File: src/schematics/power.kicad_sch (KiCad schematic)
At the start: 43 parts, among them U1 L6981NDR, U2 L6981NDR, U3 ST1S41PHR, U4 L6981NDR, U5 LM3880

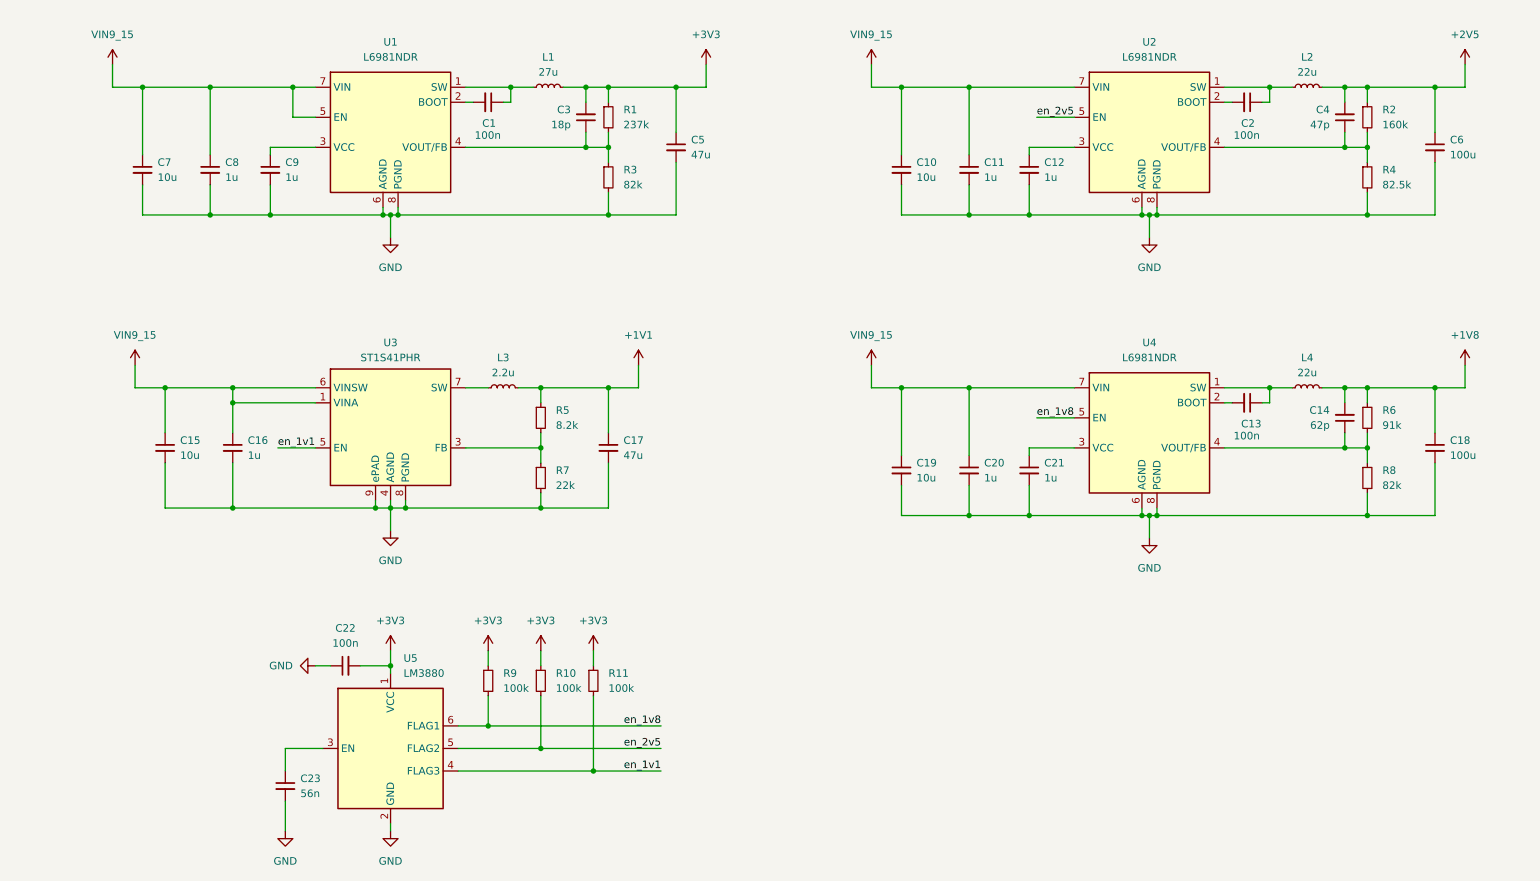
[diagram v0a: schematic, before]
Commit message: Fix some ERC issues
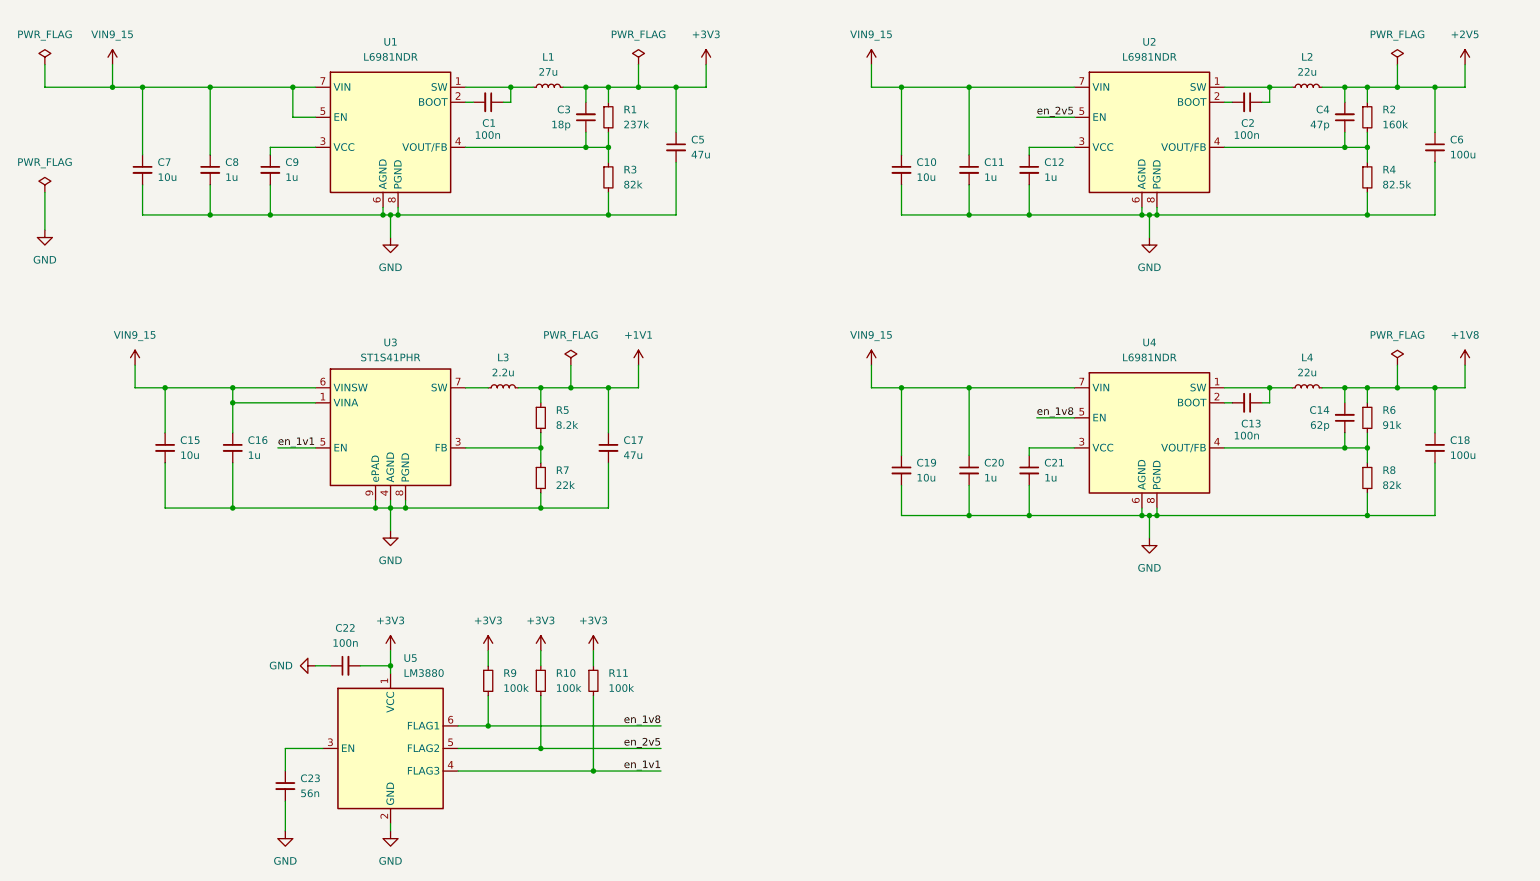
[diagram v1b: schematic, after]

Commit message: Fixes ERC issues
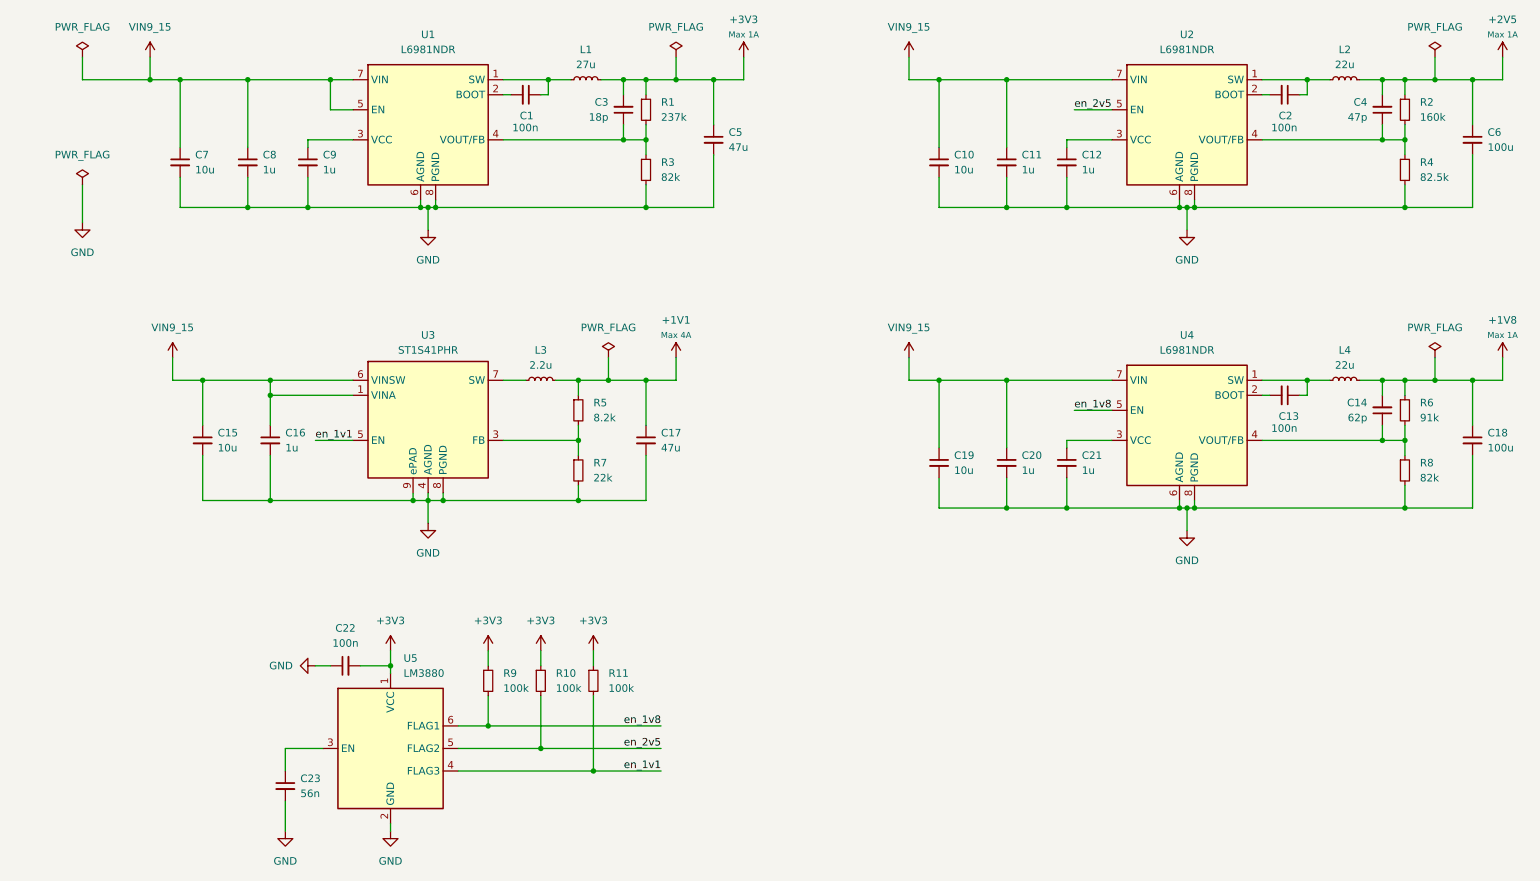
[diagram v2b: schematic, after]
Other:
- moved on the sheet: C1, C10, C11, C12, C13, C14, C15, C16, C17, C18, C19, C2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

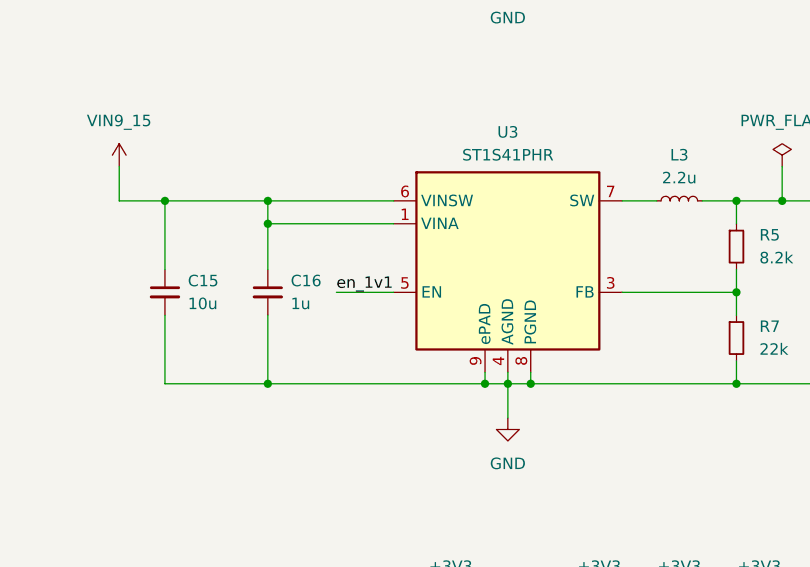
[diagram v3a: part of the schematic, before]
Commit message: ✅ Validate the Power symbols (#30)
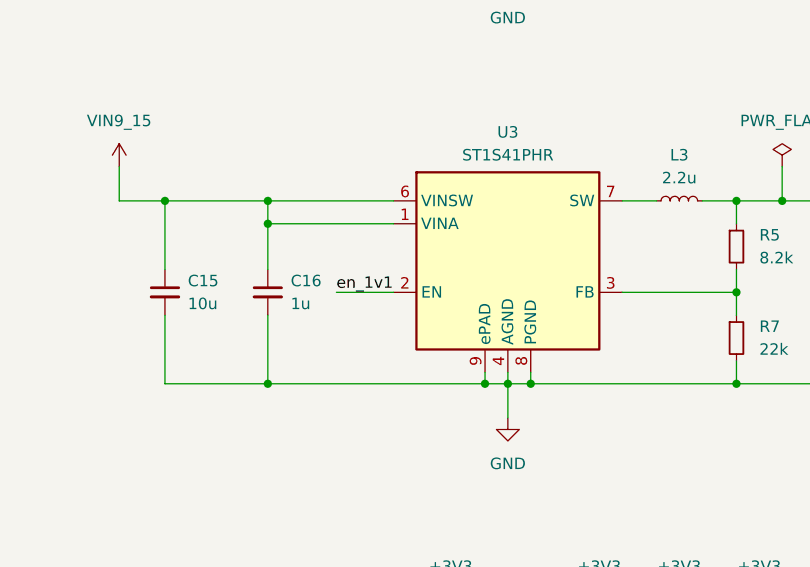
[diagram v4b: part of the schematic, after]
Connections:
- net en_1v1: now also U3.2 (EN); no longer U3.5 (EN)
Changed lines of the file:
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@@
 		(pin "5"
+		)
+		(pin "2"
 		)
 		(instances

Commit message: 🔄 Replace the eMMC IC (#34)
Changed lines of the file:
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@@
 (kicad_sch
-	(version 20231120)
+	(version 20250114)
 	(generator "eeschema")
-	(generator_version "8.0")
+	(generator_version "9.0")
 	(paper "A4")
 	(title_block

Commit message: Adds L6981 footprint (#57)
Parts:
- U1, U2, U4: footprint (none) -> ECAP5-DPROC:L6981
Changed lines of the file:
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@@
 			)
 		)
-		(property "Footprint" ""
+		(property "Footprint" "ECAP5-DPROC:L6981"
 			(at 92.075 48.26 0)
 			(effects
@@
 			)
 		)
-		(property "Footprint" ""
+		(property "Footprint" "ECAP5-DPROC:L6981"
 			(at 220.345 99.06 0)
 			(effects
@@
 			)
 		)
-		(property "Footprint" ""
+		(property "Footprint" "ECAP5-DPROC:L6981"
 			(at 220.345 48.26 0)
 			(effects
